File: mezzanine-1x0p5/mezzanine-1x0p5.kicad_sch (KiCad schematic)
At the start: 10 parts

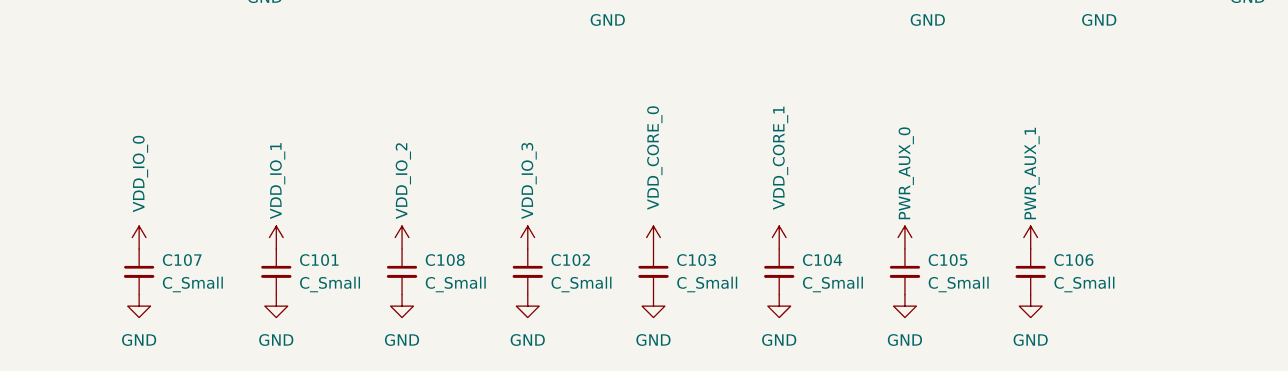
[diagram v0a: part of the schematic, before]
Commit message: create 1xp5 panel
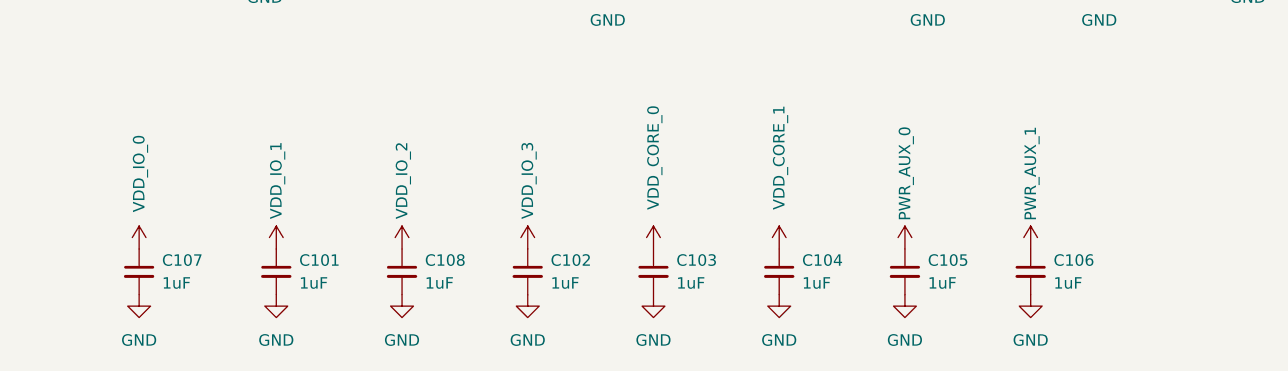
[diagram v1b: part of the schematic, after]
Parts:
- C101, C102, C103, C104, C105, C106, C107, C108: value C_Small -> 1uF
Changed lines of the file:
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@@
 			)
 		)
-		(property "Value" "C_Small"
+		(property "Value" "1uF"
 			(at 170.18 153.6762 0)
 			(show_name no)
@@
 			)
 		)
-		(property "Value" "C_Small"
+		(property "Value" "1uF"
 			(at 198.12 153.6762 0)
 			(show_name no)
@@
 			)
 		)
-		(property "Value" "C_Small"
+		(property "Value" "1uF"
 			(at 140.97 153.6762 0)
 			(show_name no)
@@
 			)
 		)
-		(property "Value" "C_Small"
+		(property "Value" "1uF"
 			(at 184.15 153.6762 0)
 			(show_name no)
@@
 			)
 		)
-		(property "Value" "C_Small"
+		(property "Value" "1uF"
 			(at 156.21 153.6762 0)
 			(show_name no)
@@
 			)
 		)
-		(property "Value" "C_Small"
+		(property "Value" "1uF"
 			(at 212.09 153.6762 0)
 			(show_name no)
@@
 			)
 		)
-		(property "Value" "C_Small"
+		(property "Value" "1uF"
 			(at 240.03 153.6762 0)
 			(show_name no)
@@
 			)
 		)
-		(property "Value" "C_Small"
+		(property "Value" "1uF"
 			(at 226.06 153.6762 0)
 			(show_name no)
